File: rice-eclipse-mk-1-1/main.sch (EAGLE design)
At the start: 102 parts, among them IC1 LMV321LICTRT, IC2 LMV321LICTRT, IC3 LMV321LICTRT, IC4 LMV321LICTRT, IC5 UA78M, IC6 LMV321LICTRT, U1 LM1084ISX-5.0/NOPB, U2 THS4531IDRD8-M, U3 THS4531IDRD8-M, U4 THS4531IDRD8-M, U5 THS4531IDRD8-M, U6 1101M2S3CQE2, U7 1101M2S3CQE2, X1 2540-5

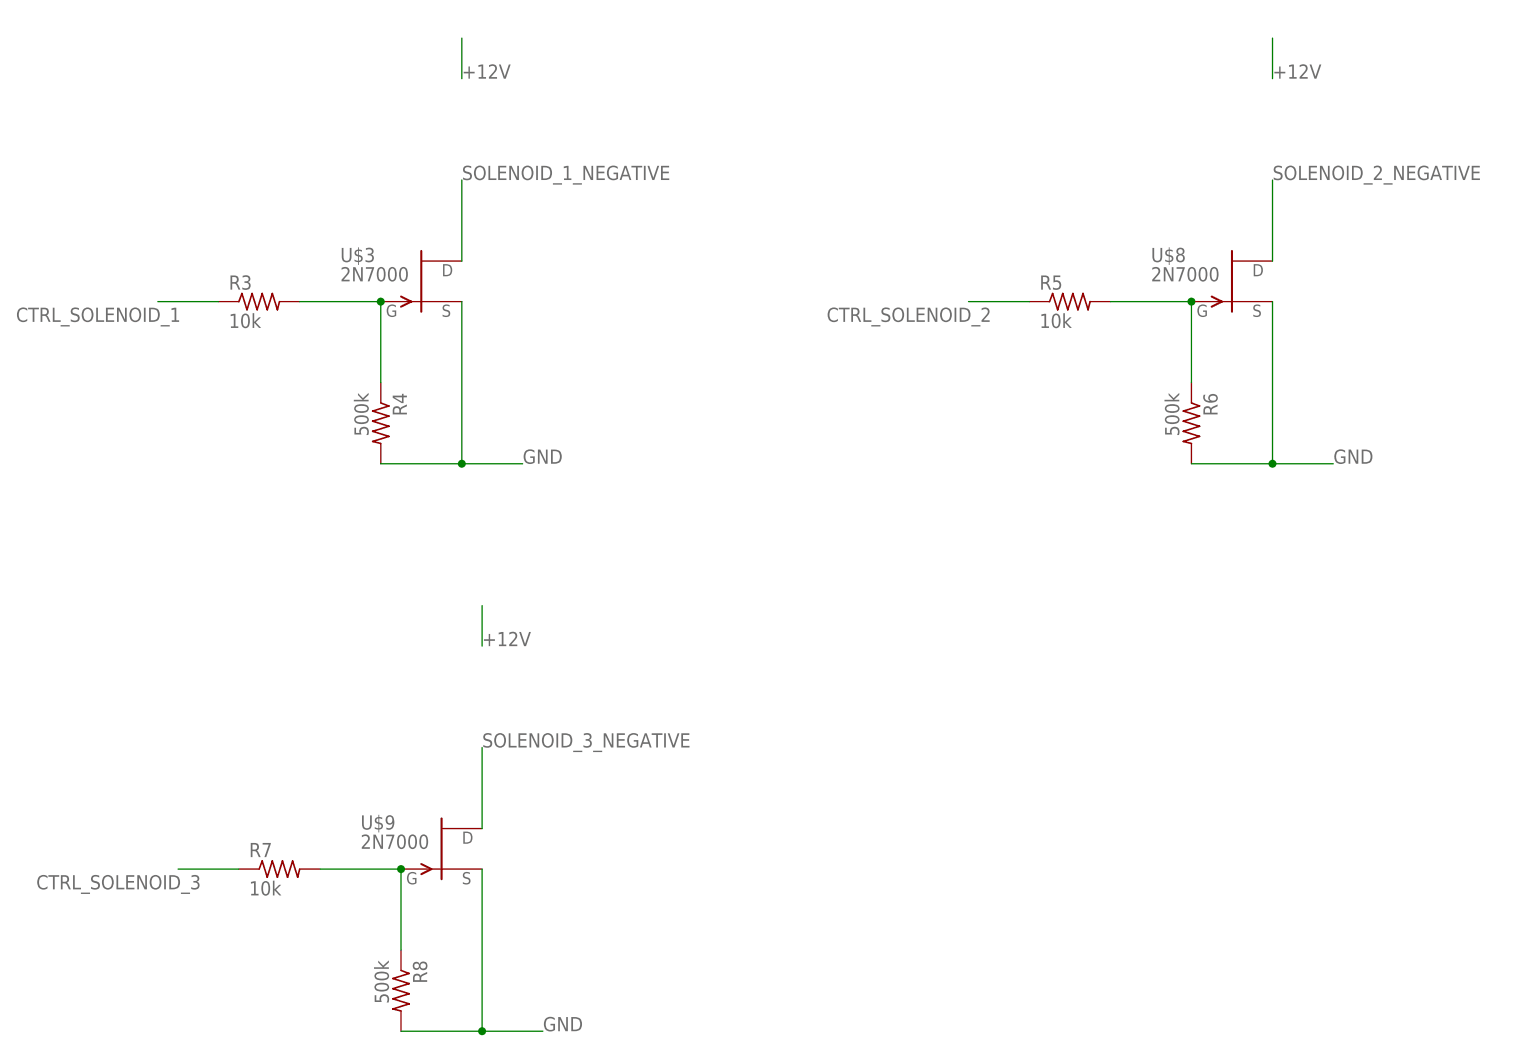
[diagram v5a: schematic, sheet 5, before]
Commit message: Added flyback diodes and moved stuff onto board.
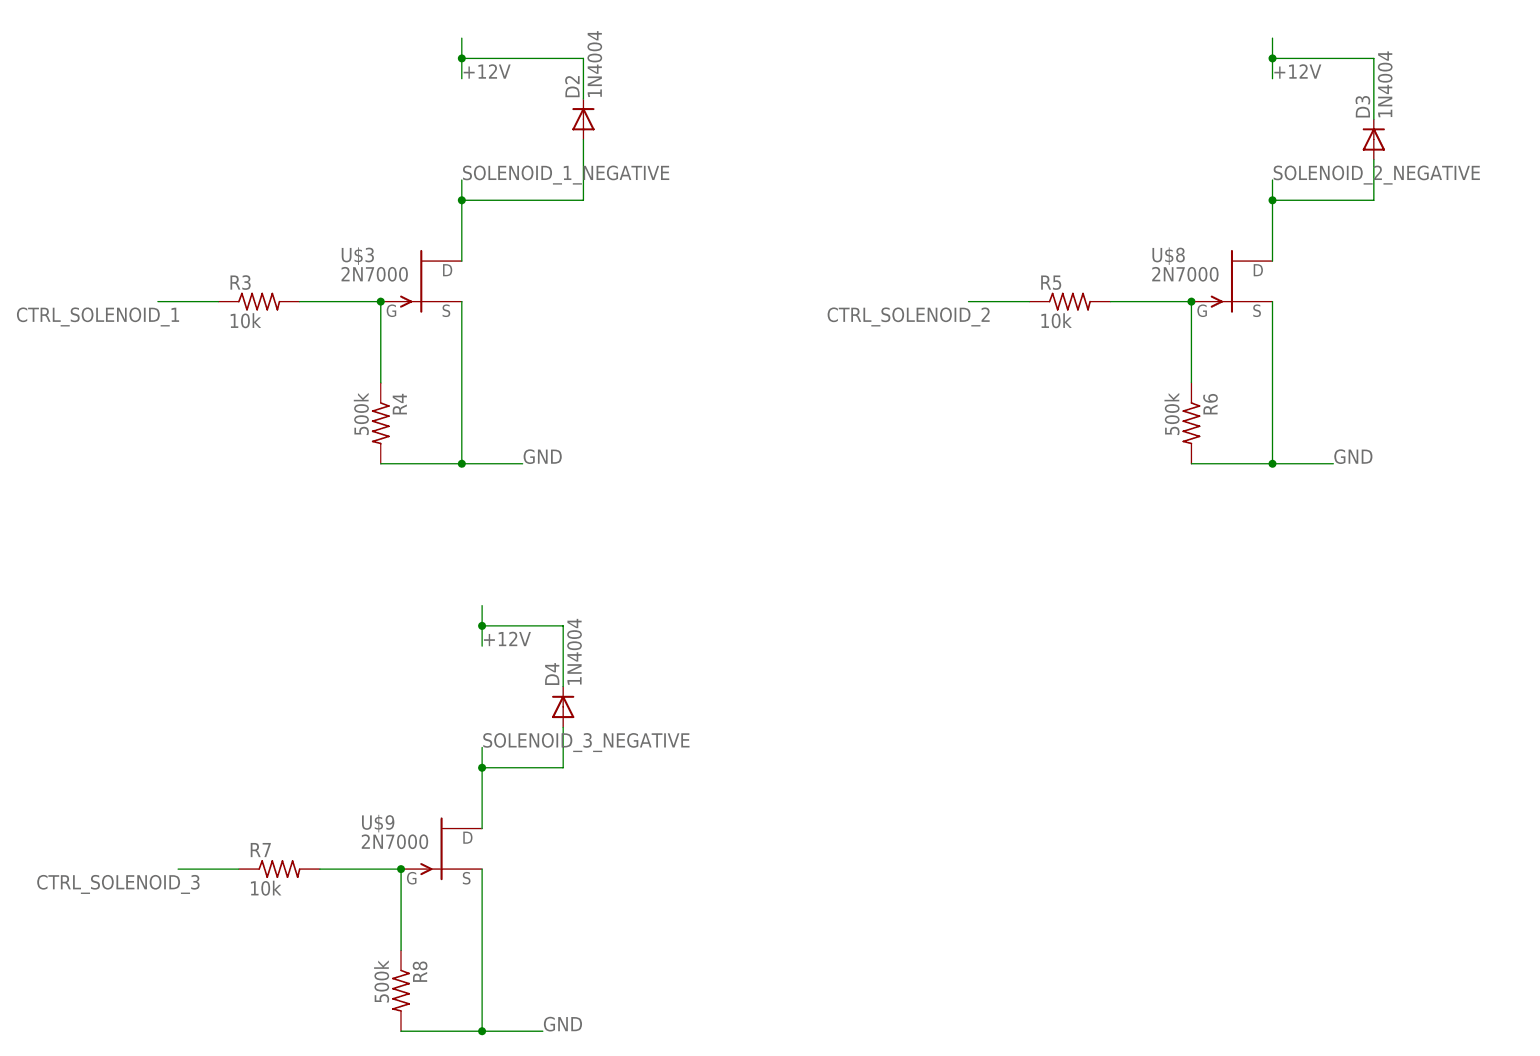
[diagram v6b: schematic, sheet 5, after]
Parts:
- removed U7: 1101M2S3CQE2, SLIDE_SW:1101M2S3CQE2
- added D1, D2, D3, D4: 1N4004, diode:1N4004
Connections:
- removed net N$4: C16.+, IC5.VO, U7.P
- net +10V: now also C16.+, IC5.VO; no longer U7.O
- net +12V: now also D1.C, D2.C, D3.C, D4.C
- net RELAY_NEGATIVE: now also D1.A
- net SOLENOID_1_NEGATIVE: now also D2.A
- net SOLENOID_2_NEGATIVE: now also D3.A
- net SOLENOID_3_NEGATIVE: now also D4.A
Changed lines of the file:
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@@
 <part name="C16" library="rcl" library_urn="urn:adsk.eagle:library:334" deviceset="CPOL-US" device="E2.5-5" package3d_urn="urn:adsk.eagle:package:23344/1" value="0.1UF"/>
 <part name="C17" library="rcl" library_urn="urn:adsk.eagle:library:334" deviceset="CPOL-US" device="E2.5-5" package3d_urn="urn:adsk.eagle:package:23344/1" value="0.33UF"/>
-<part name="U7" library="SLIDE_SW" deviceset="1101M2S3CQE2" device=""/>
 <part name="JP1" library="pinhead" library_urn="urn:adsk.eagle:library:325" deviceset="PINHD-1X2" device="" package3d_urn="urn:adsk.eagle:package:22435/2"/>
 <part name="JP2" library="pinhead" library_urn="urn:adsk.eagle:library:325" deviceset="PINHD-1X2" device="" package3d_urn="urn:adsk.eagle:package:22435/2"/>
@@
 <part name="R41" library="rcl" library_urn="urn:adsk.eagle:library:334" deviceset="R-US_" device="0204/7" package3d_urn="urn:adsk.eagle:package:23498/1" value="?"/>
 <part name="R40" library="rcl" library_urn="urn:adsk.eagle:library:334" deviceset="R-US_" device="0204/7" package3d_urn="urn:adsk.eagle:package:23498/1" value="?"/>
+<part name="D1" library="diode" library_urn="urn:adsk.eagle:library:210" deviceset="1N4004" device="" package3d_urn="urn:adsk.eagle:package:43336/1"/>
+<part name="D2" library="diode" library_urn="urn:adsk.eagle:library:210" deviceset="1N4004" device="" package3d_urn="urn:adsk.eagle:package:43336/1"/>
+<part name="D3" library="diode" library_urn="urn:adsk.eagle:library:210" deviceset="1N4004" device="" package3d_urn="urn:adsk.eagle:package:43336/1"/>
+<part name="D4" library="diode" library_urn="urn:adsk.eagle:library:210" deviceset="1N4004" device="" package3d_urn="urn:adsk.eagle:package:43336/1"/>
 </parts>
 <sheets>
@@
 <instance part="C16" gate="G$1" x="71.12" y="134.62"/>
 <instance part="C17" gate="G$1" x="43.18" y="134.62"/>
-<instance part="U7" gate="A" x="76.2" y="147.32" rot="R270"/>
 </instances>
 <busses>
@@
 <wire x1="93.98" y1="137.16" x2="119.38" y2="137.16" width="0.1524" layer="91"/>
 <label x="119.38" y="137.16" size="1.778" layer="95"/>
-<pinref part="U7" gate="A" pin="O"/>
 <junction x="93.98" y="137.16"/>
-<wire x1="81.28" y1="149.86" x2="93.98" y2="149.86" width="0.1524" layer="91"/>
+<wire x1="71.12" y1="149.86" x2="93.98" y2="149.86" width="0.1524" layer="91"/>
 <wire x1="93.98" y1="149.86" x2="93.98" y2="137.16" width="0.1524" layer="91"/>
+<pinref part="IC5" gate="G$1" pin="VO"/>
+<pinref part="C16" gate="G$1" pin="+"/>
+<wire x1="68.58" y1="137.16" x2="71.12" y2="137.16" width="0.1524" layer="91"/>
+<junction x="71.12" y="137.16"/>
+<wire x1="71.12" y1="137.16" x2="71.12" y2="149.86" width="0.1524" layer="91"/>
 </segment>
 </net>
@@
 <pinref part="LED4" gate="G$1" pin="C"/>
 <pinref part="R35" gate="G$1" pin="1"/>
-</segment>
-</net>
-<net name="N$4" class="0">
-<segment>
-<pinref part="IC5" gate="G$1" pin="VO"/>
-<pinref part="C16" gate="G$1" pin="+"/>
-<wire x1="68.58" y1="137.16" x2="71.12" y2="137.16" width="0.1524" layer="91"/>
-<pinref part="U7" gate="A" pin="P"/>
-<junction x="71.12" y="137.16"/>
-<wire x1="71.12" y1="137.16" x2="71.12" y2="147.32" width="0.1524" layer="91"/>
 </segment>
 </net>
@@
 <instance part="R7" gate="G$1" x="48.26" y="53.34"/>
 <instance part="R8" gate="G$1" x="63.5" y="38.1" rot="R270"/>
+<instance part="D2" gate="1" x="86.36" y="147.32" rot="R90"/>
+<instance part="D3" gate="1" x="185.42" y="144.78" rot="R90"/>
+<instance part="D4" gate="1" x="83.82" y="73.66" rot="R90"/>
 </instances>
 <busses>
@@
 <segment>
 <pinref part="U$3" gate="G$1" pin="D"/>
-<wire x1="71.12" y1="129.54" x2="71.12" y2="139.7" width="0.1524" layer="91"/>
+<wire x1="71.12" y1="129.54" x2="71.12" y2="137.16" width="0.1524" layer="91"/>
 <label x="71.12" y="139.7" size="1.778" layer="95"/>
+<wire x1="71.12" y1="137.16" x2="71.12" y2="139.7" width="0.1524" layer="91"/>
+<wire x1="71.12" y1="137.16" x2="86.36" y2="137.16" width="0.1524" layer="91"/>
+<junction x="71.12" y="137.16"/>
+<pinref part="D2" gate="1" pin="A"/>
+<wire x1="86.36" y1="137.16" x2="86.36" y2="144.78" width="0.1524" layer="91"/>
 </segment>
 </net>
 <net name="+12V" class="0">
 <segment>
-<wire x1="71.12" y1="157.48" x2="71.12" y2="152.4" width="0.1524" layer="91"/>
+<wire x1="71.12" y1="157.48" x2="71.12" y2="154.94" width="0.1524" layer="91"/>
 <label x="71.12" y="152.4" size="1.778" layer="95"/>
-</segment>
-<segment>
-<wire x1="172.72" y1="157.48" x2="172.72" y2="152.4" width="0.1524" layer="91"/>
+<pinref part="D2" gate="1" pin="C"/>
+<wire x1="71.12" y1="154.94" x2="71.12" y2="152.4" width="0.1524" layer="91"/>
+<wire x1="86.36" y1="149.86" x2="86.36" y2="154.94" width="0.1524" layer="91"/>
+<wire x1="86.36" y1="154.94" x2="71.12" y2="154.94" width="0.1524" layer="91"/>
+<junction x="71.12" y="154.94"/>
+</segment>
+<segment>
+<wire x1="172.72" y1="157.48" x2="172.72" y2="154.94" width="0.1524" layer="91"/>
 <label x="172.72" y="152.4" size="1.778" layer="95"/>
-</segment>
-<segment>
-<wire x1="73.66" y1="86.36" x2="73.66" y2="81.28" width="0.1524" layer="91"/>
+<pinref part="D3" gate="1" pin="C"/>
+<wire x1="172.72" y1="154.94" x2="172.72" y2="152.4" width="0.1524" layer="91"/>
+<wire x1="185.42" y1="147.32" x2="185.42" y2="154.94" width="0.1524" layer="91"/>
+<wire x1="185.42" y1="154.94" x2="172.72" y2="154.94" width="0.1524" layer="91"/>
+<junction x="172.72" y="154.94"/>
+</segment>
+<segment>
+<wire x1="73.66" y1="86.36" x2="73.66" y2="83.82" width="0.1524" layer="91"/>
 <label x="73.66" y="81.28" size="1.778" layer="95"/>
+<pinref part="D4" gate="1" pin="C"/>
+<wire x1="73.66" y1="83.82" x2="73.66" y2="81.28" width="0.1524" layer="91"/>
+<wire x1="83.82" y1="76.2" x2="83.82" y2="83.82" width="0.1524" layer="91"/>
+<wire x1="83.82" y1="83.82" x2="73.66" y2="83.82" width="0.1524" layer="91"/>
+<junction x="73.66" y="83.82"/>
 </segment>
 </net>
@@
 <segment>
 <pinref part="U$8" gate="G$1" pin="D"/>
-<wire x1="172.72" y1="129.54" x2="172.72" y2="139.7" width="0.1524" layer="91"/>
+<wire x1="172.72" y1="129.54" x2="172.72" y2="137.16" width="0.1524" layer="91"/>
 <label x="172.72" y="139.7" size="1.778" layer="95"/>
+<pinref part="D3" gate="1" pin="A"/>
+<wire x1="172.72" y1="137.16" x2="172.72" y2="139.7" width="0.1524" layer="91"/>
+<wire x1="172.72" y1="137.16" x2="185.42" y2="137.16" width="0.1524" layer="91"/>
+<wire x1="185.42" y1="137.16" x2="185.42" y2="142.24" width="0.1524" layer="91"/>
+<junction x="172.72" y="137.16"/>
 </segment>
 </net>
@@
 <segment>
 <pinref part="U$9" gate="G$1" pin="D"/>
-<wire x1="73.66" y1="58.42" x2="73.66" y2="68.58" width="0.1524" layer="91"/>
+<wire x1="73.66" y1="58.42" x2="73.66" y2="66.04" width="0.1524" layer="91"/>
 <label x="73.66" y="68.58" size="1.778" layer="95"/>
+<pinref part="D4" gate="1" pin="A"/>
+<wire x1="73.66" y1="66.04" x2="73.66" y2="68.58" width="0.1524" layer="91"/>
+<wire x1="73.66" y1="66.04" x2="83.82" y2="66.04" width="0.1524" layer="91"/>
+<wire x1="83.82" y1="66.04" x2="83.82" y2="71.12" width="0.1524" layer="91"/>
+<junction x="73.66" y="66.04"/>
 </segment>
 </net>
@@
 <instance part="R1" gate="G$1" x="99.06" y="104.14"/>
 <instance part="R2" gate="G$1" x="114.3" y="88.9" rot="R270"/>
+<instance part="D1" gate="1" x="149.86" y="119.38" rot="R90"/>
 </instances>
 <busses>
@@
 <wire x1="124.46" y1="109.22" x2="124.46" y2="119.38" width="0.1524" layer="91"/>
 <label x="124.46" y="116.84" size="1.778" layer="95"/>
+<pinref part="D1" gate="1" pin="A"/>
+<wire x1="124.46" y1="109.22" x2="149.86" y2="109.22" width="0.1524" layer="91"/>
+<wire x1="149.86" y1="109.22" x2="149.86" y2="116.84" width="0.1524" layer="91"/>
+<junction x="124.46" y="109.22"/>
 </segment>
 </net>
 <net name="+12V" class="0">
 <segment>
-<wire x1="124.46" y1="134.62" x2="124.46" y2="129.54" width="0.1524" layer="91"/>
+<wire x1="124.46" y1="134.62" x2="124.46" y2="132.08" width="0.1524" layer="91"/>
 <label x="124.46" y="129.54" size="1.778" layer="95"/>
-</segment>
-</net>
+<pinref part="D1" gate="1" pin="C"/>
+<wire x1="124.46" y1="132.08" x2="124.46" y2="129.54" width="0.1524" layer="91"/>
+<wire x1="149.86" y1="121.92" x2="149.86" y2="132.08" width="0.1524" layer="91"/>
+<wire x1="149.86" y1="132.08" x2="124.46" y2="132.08" width="0.1524" layer="91"/>
+<junction x="124.46" y="132.08"/>
+</segment>
+</net>

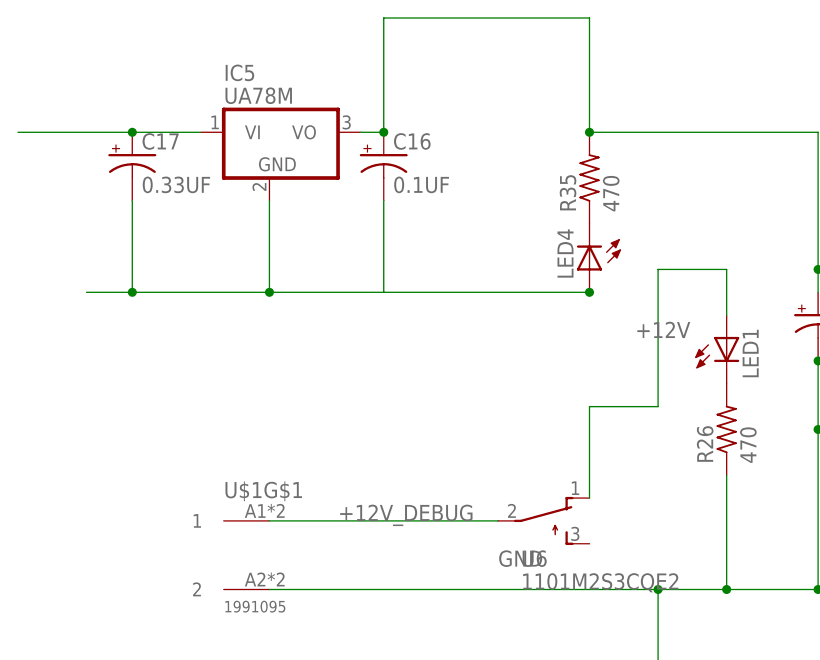
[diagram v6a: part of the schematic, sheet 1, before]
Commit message: Added schottky diode.
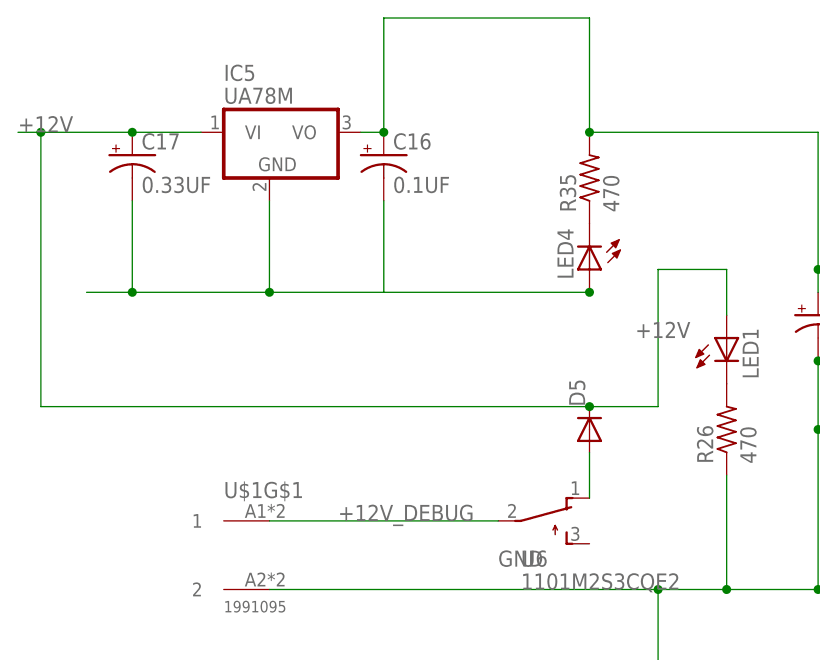
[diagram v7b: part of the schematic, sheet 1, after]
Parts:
- added D5: (no value), diode:DIODE-DO201-15
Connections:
- new net N$4: D5.A, U6.O
- net +12V: now also D5.C; no longer U6.O
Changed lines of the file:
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@@
 <part name="D3" library="diode" library_urn="urn:adsk.eagle:library:210" deviceset="1N4004" device="" package3d_urn="urn:adsk.eagle:package:43336/1"/>
 <part name="D4" library="diode" library_urn="urn:adsk.eagle:library:210" deviceset="1N4004" device="" package3d_urn="urn:adsk.eagle:package:43336/1"/>
+<part name="D5" library="diode" library_urn="urn:adsk.eagle:library:210" deviceset="DIODE-" device="DO201-15" package3d_urn="urn:adsk.eagle:package:43365/1"/>
 </parts>
 <sheets>
@@
 <instance part="C16" gate="G$1" x="71.12" y="134.62"/>
 <instance part="C17" gate="G$1" x="43.18" y="134.62"/>
+<instance part="D5" gate="G$1" x="93.98" y="104.14" rot="R90"/>
 </instances>
 <busses>
@@
 <segment>
 <label x="99.06" y="114.3" size="1.778" layer="95"/>
-<wire x1="93.98" y1="106.68" x2="101.6" y2="106.68" width="0.1524" layer="91"/>
 <wire x1="101.6" y1="106.68" x2="101.6" y2="121.92" width="0.1524" layer="91"/>
-<pinref part="U6" gate="A" pin="O"/>
-<wire x1="93.98" y1="96.52" x2="93.98" y2="106.68" width="0.1524" layer="91"/>
 <pinref part="LED1" gate="G$1" pin="A"/>
 <wire x1="109.22" y1="121.92" x2="109.22" y2="116.84" width="0.1524" layer="91"/>
 <wire x1="101.6" y1="121.92" x2="109.22" y2="121.92" width="0.1524" layer="91"/>
-</segment>
-<segment>
 <pinref part="IC5" gate="G$1" pin="VI"/>
 <wire x1="50.8" y1="137.16" x2="43.18" y2="137.16" width="0.1524" layer="91"/>
 <pinref part="C17" gate="G$1" pin="+"/>
-<wire x1="43.18" y1="137.16" x2="30.48" y2="137.16" width="0.1524" layer="91"/>
+<wire x1="43.18" y1="137.16" x2="33.02" y2="137.16" width="0.1524" layer="91"/>
 <junction x="43.18" y="137.16"/>
+<label x="30.48" y="137.16" size="1.778" layer="95"/>
+<wire x1="33.02" y1="137.16" x2="30.48" y2="137.16" width="0.1524" layer="91"/>
+<wire x1="101.6" y1="106.68" x2="93.98" y2="106.68" width="0.1524" layer="91"/>
+<wire x1="93.98" y1="106.68" x2="33.02" y2="106.68" width="0.1524" layer="91"/>
+<wire x1="33.02" y1="106.68" x2="33.02" y2="137.16" width="0.1524" layer="91"/>
+<junction x="33.02" y="137.16"/>
+<pinref part="D5" gate="G$1" pin="C"/>
+<junction x="93.98" y="106.68"/>
 </segment>
 </net>
@@
 </segment>
 </net>
+<net name="N$4" class="0">
+<segment>
+<pinref part="D5" gate="G$1" pin="A"/>
+<pinref part="U6" gate="A" pin="O"/>
+<wire x1="93.98" y1="101.6" x2="93.98" y2="96.52" width="0.1524" layer="91"/>
+</segment>
+</net>

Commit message: Added some stuff.
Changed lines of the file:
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@@
 <wire x1="71.12" y1="119.38" x2="93.98" y2="119.38" width="0.1524" layer="91"/>
 <junction x="93.98" y="119.38"/>
+<junction x="71.12" y="119.38"/>
+<label x="38.1" y="119.38" size="1.778" layer="95"/>
 </segment>
 </net>
@@
 <wire x1="63.5" y1="165.1" x2="76.2" y2="165.1" width="0.1524" layer="91"/>
 <junction x="76.2" y="165.1"/>
-</segment>
-</net>
+<junction x="101.6" y="83.82"/>
+</segment>
+</net>
